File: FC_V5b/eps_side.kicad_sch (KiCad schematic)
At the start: 67 parts, among them IC6 LT3652IMSE#PBF, J10 INHIBIT_P2, J11 DF11CZ-12DP-2V(27), J14 Battery Input, J17 Face4 (Z- Face), J19 ISS_INHIBIT, J2 DF11CZ-12DP-2V(27), J20 RBF_Inhibit, J21 Heater Output, J29 INHIBIT_S2, J7 INHIBIT_P1, J8 INHIBIT_S1, U10 TPS54226PWPRPWP14_2P31X2P46-L, U13 TPS7A4501DCQT, U14 INA219AxD, U15 INA219AxD, U17 LMC555CMX/NOPB, U20 74LVC1G04, U9 MCP23017_SS

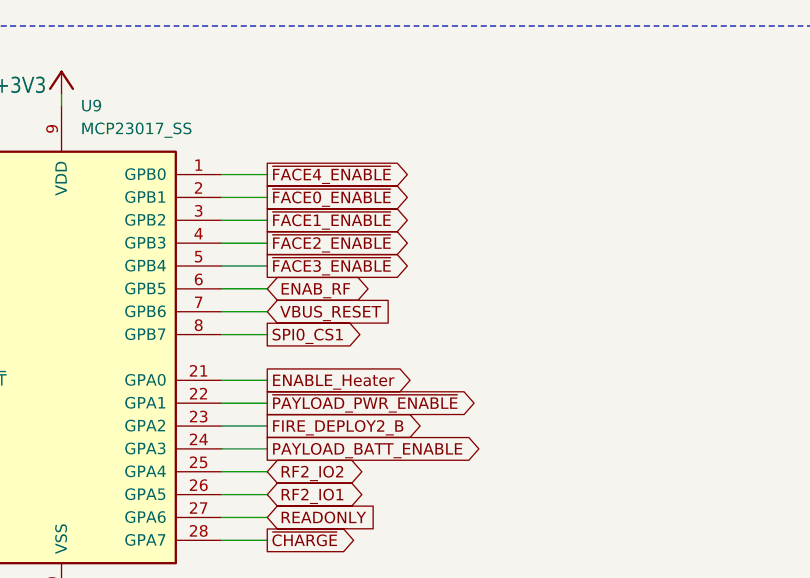
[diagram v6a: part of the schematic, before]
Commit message: Changed to AP22653AW6-7 Load Switches for EN High
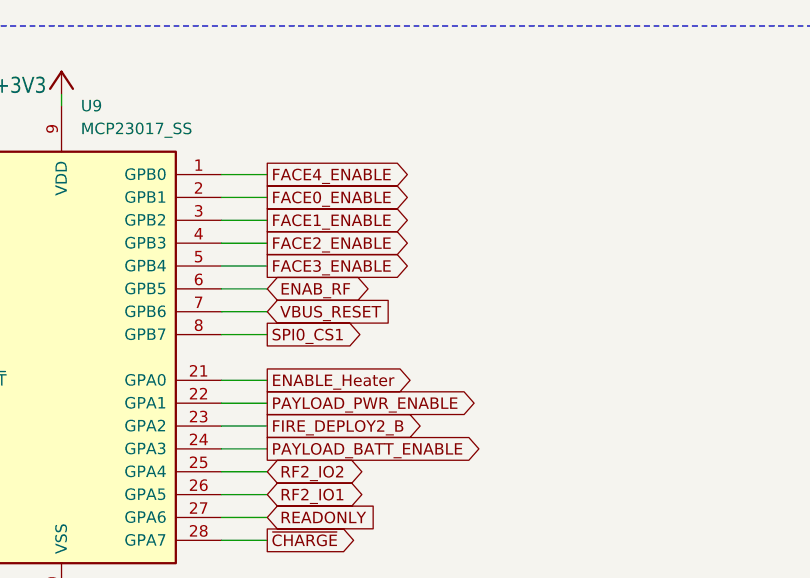
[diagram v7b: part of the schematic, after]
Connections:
- net ~{FACE0_ENABLE} renamed FACE0_ENABLE
- net ~{FACE1_ENABLE} renamed FACE1_ENABLE
- net ~{FACE2_ENABLE} renamed FACE2_ENABLE
- net ~{FACE3_ENABLE} renamed FACE3_ENABLE
- net ~{FACE4_ENABLE} renamed FACE4_ENABLE
- net ~{PAYLOAD_PWR_ENABLE} renamed PAYLOAD_PWR_ENABLE
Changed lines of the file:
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@@
 		)
 	)
-	(global_label "~{FACE2_ENABLE}"
+	(global_label "FACE2_ENABLE"
 		(shape output)
 		(at 97.79 166.37 0)
@@
 		)
 	)
-	(global_label "~{PAYLOAD_PWR_ENABLE}"
+	(global_label "PAYLOAD_PWR_ENABLE"
 		(shape output)
 		(at 97.79 184.15 0)
@@
 		)
 	)
-	(global_label "~{FACE3_ENABLE}"
+	(global_label "FACE3_ENABLE"
 		(shape output)
 		(at 97.79 168.91 0)
@@
 		)
 	)
-	(global_label "~{FACE1_ENABLE}"
+	(global_label "FACE1_ENABLE"
 		(shape output)
 		(at 97.79 163.83 0)
@@
 		)
 	)
-	(global_label "~{FACE4_ENABLE}"
+	(global_label "FACE4_ENABLE"
 		(shape output)
 		(at 97.79 158.75 0)
@@
 		)
 	)
-	(global_label "~{FACE0_ENABLE}"
+	(global_label "FACE0_ENABLE"
 		(shape output)
 		(at 97.79 161.29 0)

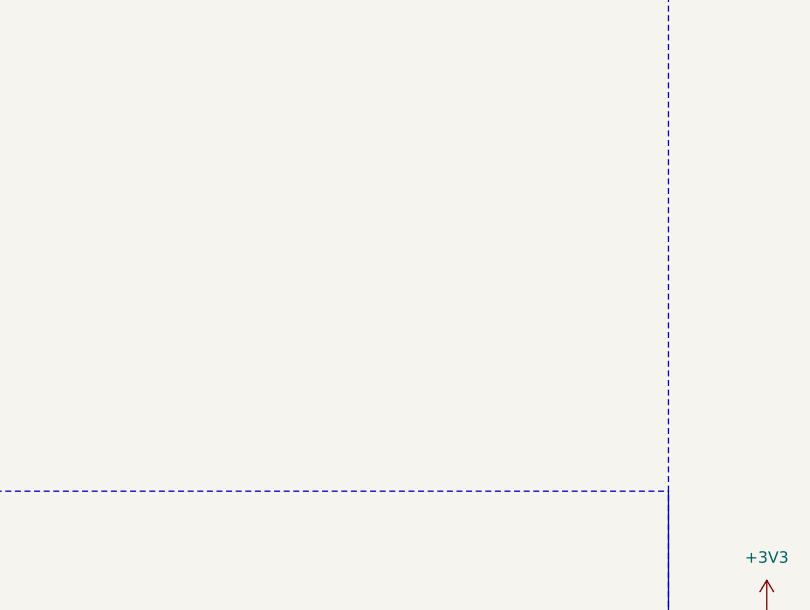
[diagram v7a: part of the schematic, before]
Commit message: Added Aux Deploy and Deploy 2 Ports
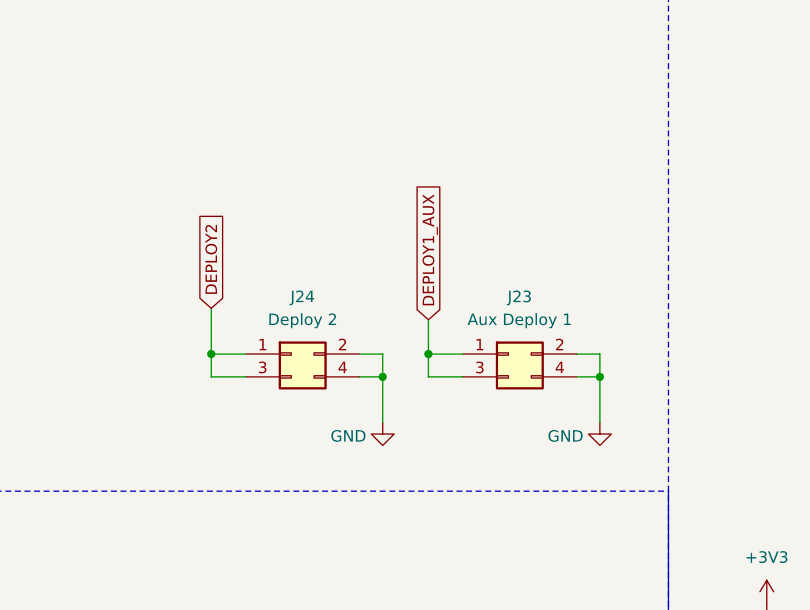
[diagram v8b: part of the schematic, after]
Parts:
- added J23: Aux Deploy 1, Connector_Hirose:Hirose_DF11-4DP-2DSA_2x02_P2.00mm_Vertical, symbol Connector_Generic:Conn_02x02_Odd_Even
- added J24: Deploy 2, Connector_Hirose:Hirose_DF11-4DP-2DSA_2x02_P2.00mm_Vertical, symbol Connector_Generic:Conn_02x02_Odd_Even
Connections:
- net GND: now also J23.2 (Pin_2), J23.4 (Pin_4), J24.2 (Pin_2), J24.4 (Pin_4)
- new net DEPLOY1_AUX: J23.1 (Pin_1), J23.3 (Pin_3)
- new net DEPLOY2: J24.1 (Pin_1), J24.3 (Pin_3)
